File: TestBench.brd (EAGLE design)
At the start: 140 x 138.5 mm, 12 parts

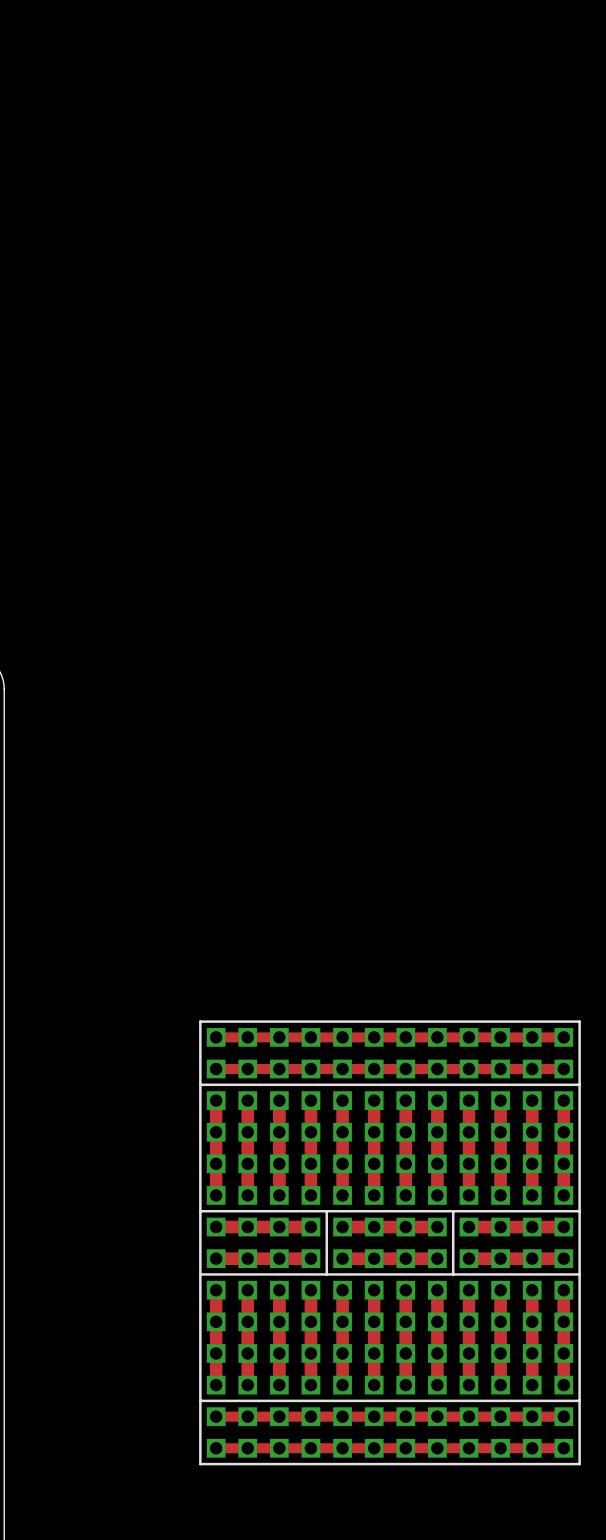
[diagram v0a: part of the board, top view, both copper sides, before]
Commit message: Renamed LogicThingie to SonicScrewdriver - cosmetic changes, panel exports, cam folders
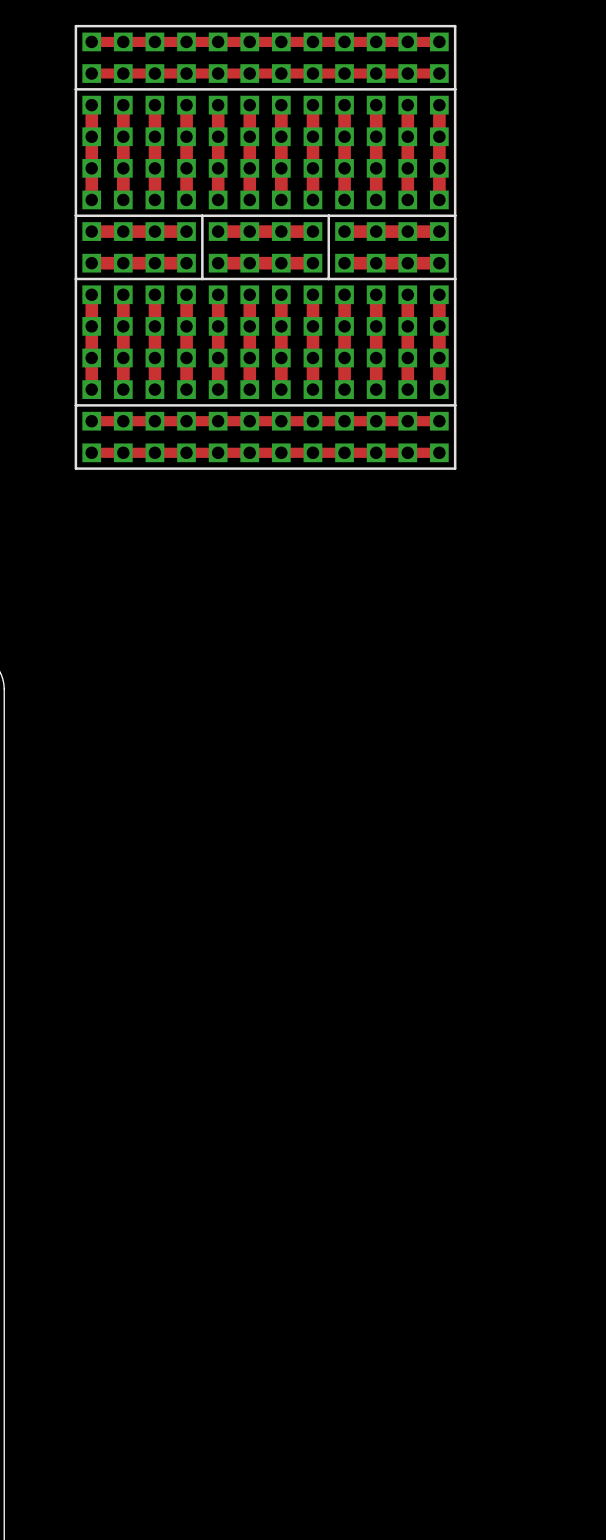
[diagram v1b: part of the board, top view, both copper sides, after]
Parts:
- moved U$3 80.6 mm to (161.0, 171.0)
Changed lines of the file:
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@@
 <element name="U$2" library="EurorackModularParts" package="POWER_16" value="POWER" x="125.73" y="115.57" rot="R270"/>
 <element name="J1" library="dp_devices" package="DC_BARREL_JACK_PTH_2MM" value="" x="129" y="135" rot="R180"/>
-<element name="U$3" library="zephod-components" package="PROTO_10_24" value="PROTOAREA" x="171" y="91"/>
+<element name="U$3" library="zephod-components" package="PROTO_10_24" value="PROTOAREA" x="161" y="171"/>
 <element name="U$4" library="EurorackModularParts" package="OG-POTS_ALPS_POT_VERTICAL" value="" x="130" y="15"/>
 <element name="U$5" library="EurorackModularParts" package="OG-POTS_ALPS_POT_VERTICAL" value="" x="130" y="35"/>
